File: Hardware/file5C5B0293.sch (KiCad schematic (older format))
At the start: 23 parts, among them J16 Conn_01x06_Male, J17 Conn_ARM_JTAG_SWD_10

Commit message: Fixed footprints for new attenuverter pots
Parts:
- gave numbers to parts that had none: 5
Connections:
- net GND: now also U13.12 (VSSA)
- no-connect marks 5 -> 13
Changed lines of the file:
@@
 SHAPE_SW
 $Comp
-L MCU_ST_STM32F3:STM32F303RBTx U?
+L MCU_ST_STM32F3:STM32F303RBTx U13
 U 1 1 5BDFE304
 P 6800 3550
-F 0 "U?" H 6800 1664 50  0000 C CNN
+F 0 "U13" H 6800 1664 50  0000 C CNN
 F 1 "STM32F303RBTx" H 6800 1573 50  0000 C CNN
 F 2 "Package_QFP:LQFP-64_10x10mm_P0.5mm" H 6200 1850 50  0001 R CNN
@@
 $EndComp
 $Comp
-L power:+3.3V #PWR?
+L power:+3.3V #PWR0155
 U 1 1 5BE1EF17
 P 3500 5850
-F 0 "#PWR?" H 3500 5700 50  0001 C CNN
+F 0 "#PWR0155" H 3500 5700 50  0001 C CNN
 F 1 "+3.3V" H 3515 6023 50  0000 C CNN
 F 2 "" H 3500 5850 50  0001 C CNN
@@
 	3500 5850 3500 5900
 $Comp
-L power:GND #PWR?
+L power:GND #PWR0156
 U 1 1 5BE1EF1E
 P 3500 6400
-F 0 "#PWR?" H 3500 6150 50  0001 C CNN
+F 0 "#PWR0156" H 3500 6150 50  0001 C CNN
 F 1 "GND" H 3505 6227 50  0000 C CNN
 F 2 "" H 3500 6400 50  0001 C CNN
@@
 $EndComp
 $Comp
-L Device:C C?
+L Device:C C72
 U 1 1 5BE1EF24
 P 2700 6100
-F 0 "C?" H 2815 6146 50  0000 L CNN
+F 0 "C72" H 2815 6146 50  0000 L CNN
 F 1 "100 nF" H 2815 6055 50  0000 L CNN
 F 2 "Capacitor_SMD:C_0603_1608Metric" H 2738 5950 50  0001 C CNN
@@
 $EndComp
 $Comp
-L Device:C C?
+L Device:C C73
 U 1 1 5BE1EF2B
 P 3200 6100
-F 0 "C?" H 3315 6146 50  0000 L CNN
+F 0 "C73" H 3315 6146 50  0000 L CNN
 F 1 "100 nF" H 3315 6055 50  0000 L CNN
 F 2 "Capacitor_SMD:C_0603_1608Metric" H 3238 5950 50  0001 C CNN
@@
 $EndComp
 $Comp
-L Device:C C?
+L Device:C C74
 U 1 1 5BE1EF32
 P 3700 6100
-F 0 "C?" H 3815 6146 50  0000 L CNN
+F 0 "C74" H 3815 6146 50  0000 L CNN
 F 1 "100 nF" H 3815 6055 50  0000 L CNN
 F 2 "Capacitor_SMD:C_0603_1608Metric" H 3738 5950 50  0001 C CNN
@@
 $EndComp
 $Comp
-L Device:CP C?
+L Device:CP C75
 U 1 1 5BE1EF39
 P 4250 6100
-F 0 "C?" H 4368 6146 50  0000 L CNN
+F 0 "C75" H 4368 6146 50  0000 L CNN
 F 1 "4.7 uF" H 4368 6055 50  0000 L CNN
 F 2 "Capacitor_Tantalum_SMD:CP_EIA-3216-18_Kemet-A" H 4288 5950 50  0001 C CNN
@@
 Wire Wire Line
 	7500 2850 7900 2850
+NoConn ~ 6100 3450
+NoConn ~ 6100 4850
+NoConn ~ 7500 4550
+NoConn ~ 7500 4450
+NoConn ~ 7500 4350
+NoConn ~ 7500 4250
+NoConn ~ 7500 4050
+Wire Wire Line
+	6900 5650 7000 5650
+Wire Wire Line
+	7000 5650 7000 5350
+Connection ~ 6900 5650
+NoConn ~ 6600 1750
 $EndSCHEMATC

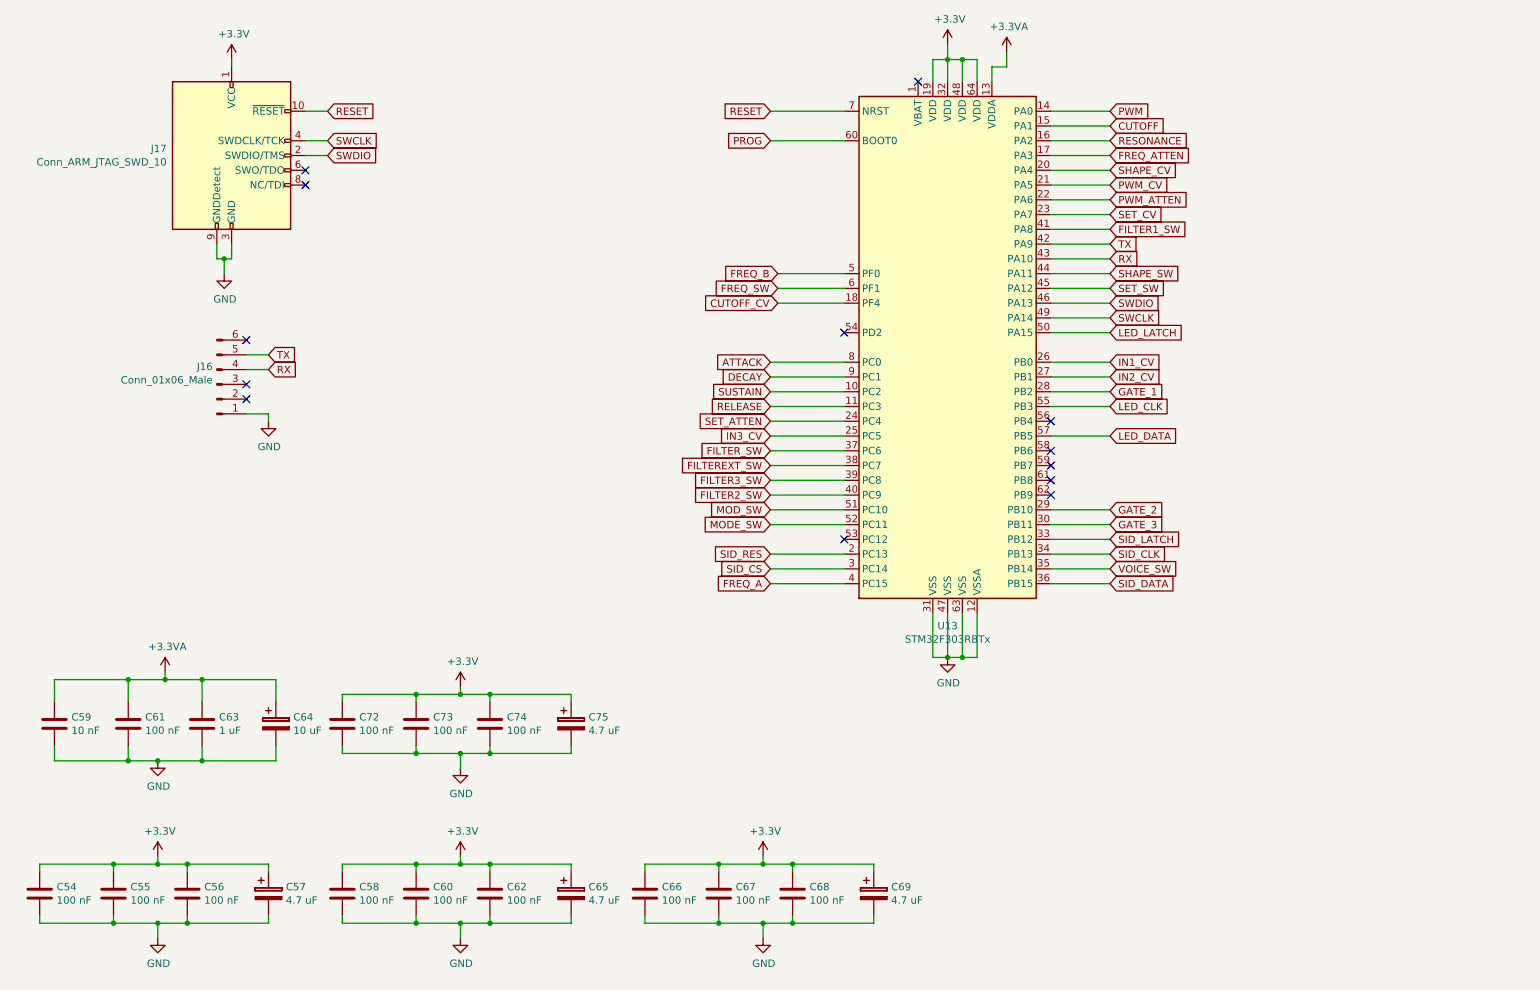
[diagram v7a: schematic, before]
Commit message: Seperated two board with headers
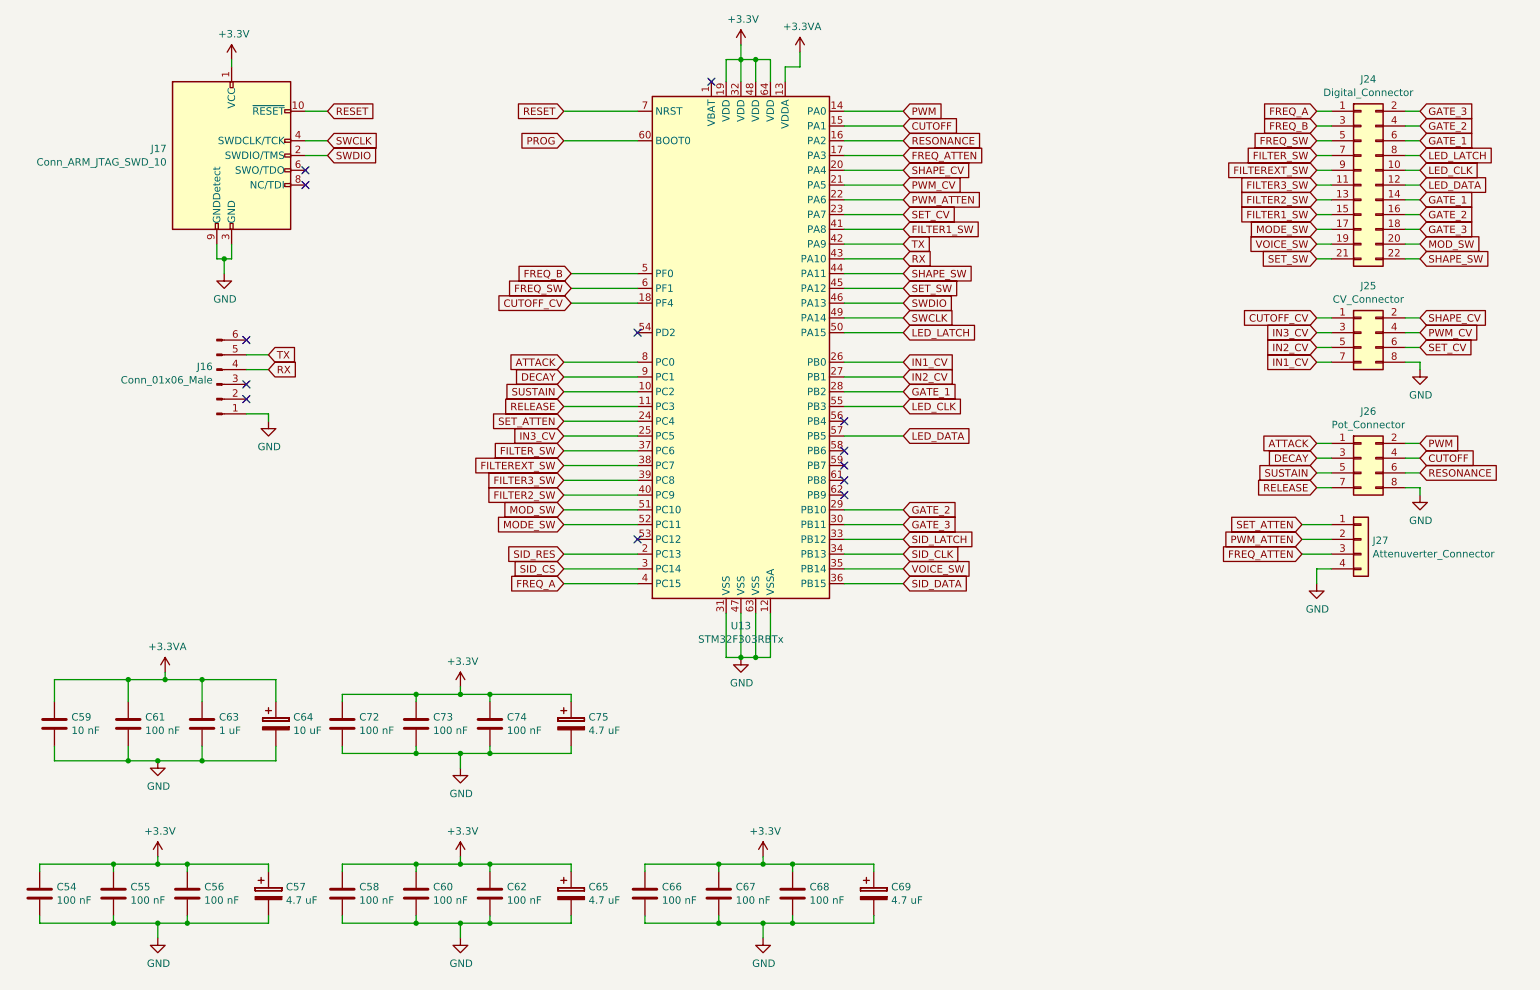
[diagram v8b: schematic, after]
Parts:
- added J24: Digital_Connector, Connector_PinHeader_2.54mm:PinHeader_2x11_P2.54mm_Vertical, symbol Connector_Generic:Conn_02x11_Odd_Even
- added J25: CV_Connector, Connector_PinSocket_2.54mm:PinSocket_2x04_P2.54mm_Vertical, symbol Connector_Generic:Conn_02x04_Odd_Even
- added J26: Pot_Connector, Connector_PinSocket_2.54mm:PinSocket_2x04_P2.54mm_Vertical, symbol Connector_Generic:Conn_02x04_Odd_Even
- added J27: Attenuverter_Connector, Connector_PinSocket_2.54mm:PinSocket_1x04_P2.54mm_Vertical, symbol Connector_Generic:Conn_01x04
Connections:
- net ATTACK: now also J26.1 (Pin_1)
- net CUTOFF: now also J26.4 (Pin_4)
- net CUTOFF_CV: now also J25.1 (Pin_1)
- net DECAY: now also J26.3 (Pin_3)
- net FILTER1_SW: now also J24.15 (Pin_15)
- net FILTER2_SW: now also J24.13 (Pin_13)
- net FILTER3_SW: now also J24.11 (Pin_11)
- net FILTEREXT_SW: now also J24.9 (Pin_9)
- net FILTER_SW: now also J24.7 (Pin_7)
- net FREQ_A: now also J24.1 (Pin_1)
- net FREQ_ATTEN: now also J27.3 (Pin_3)
- net FREQ_B: now also J24.3 (Pin_3)
- net FREQ_SW: now also J24.5 (Pin_5)
- net GATE_1: now also J24.14 (Pin_14), J24.6 (Pin_6)
- net GATE_2: now also J24.16 (Pin_16), J24.4 (Pin_4)
- net GATE_3: now also J24.18 (Pin_18), J24.2 (Pin_2)
- net GND: now also J25.8 (Pin_8), J26.8 (Pin_8), J27.4 (Pin_4)
- net IN1_CV: now also J25.7 (Pin_7)
- net IN2_CV: now also J25.5 (Pin_5)
- net IN3_CV: now also J25.3 (Pin_3)
- net LED_CLK: now also J24.10 (Pin_10)
- net LED_DATA: now also J24.12 (Pin_12)
- net LED_LATCH: now also J24.8 (Pin_8)
- net MODE_SW: now also J24.17 (Pin_17)
- net MOD_SW: now also J24.20 (Pin_20)
- net PWM: now also J26.2 (Pin_2)
- net PWM_ATTEN: now also J27.2 (Pin_2)
- net PWM_CV: now also J25.4 (Pin_4)
- net RELEASE: now also J26.7 (Pin_7)
- net RESONANCE: now also J26.6 (Pin_6)
- net SET_ATTEN: now also J27.1 (Pin_1)
- net SET_CV: now also J25.6 (Pin_6)
- net SET_SW: now also J24.21 (Pin_21)
- net SHAPE_CV: now also J25.2 (Pin_2)
- net SHAPE_SW: now also J24.22 (Pin_22)
- net SUSTAIN: now also J26.5 (Pin_5)
- net VOICE_SW: now also J24.19 (Pin_19)
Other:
- moved on the sheet: U13
